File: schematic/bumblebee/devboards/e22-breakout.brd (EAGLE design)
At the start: 100 x 80 mm, 3 parts

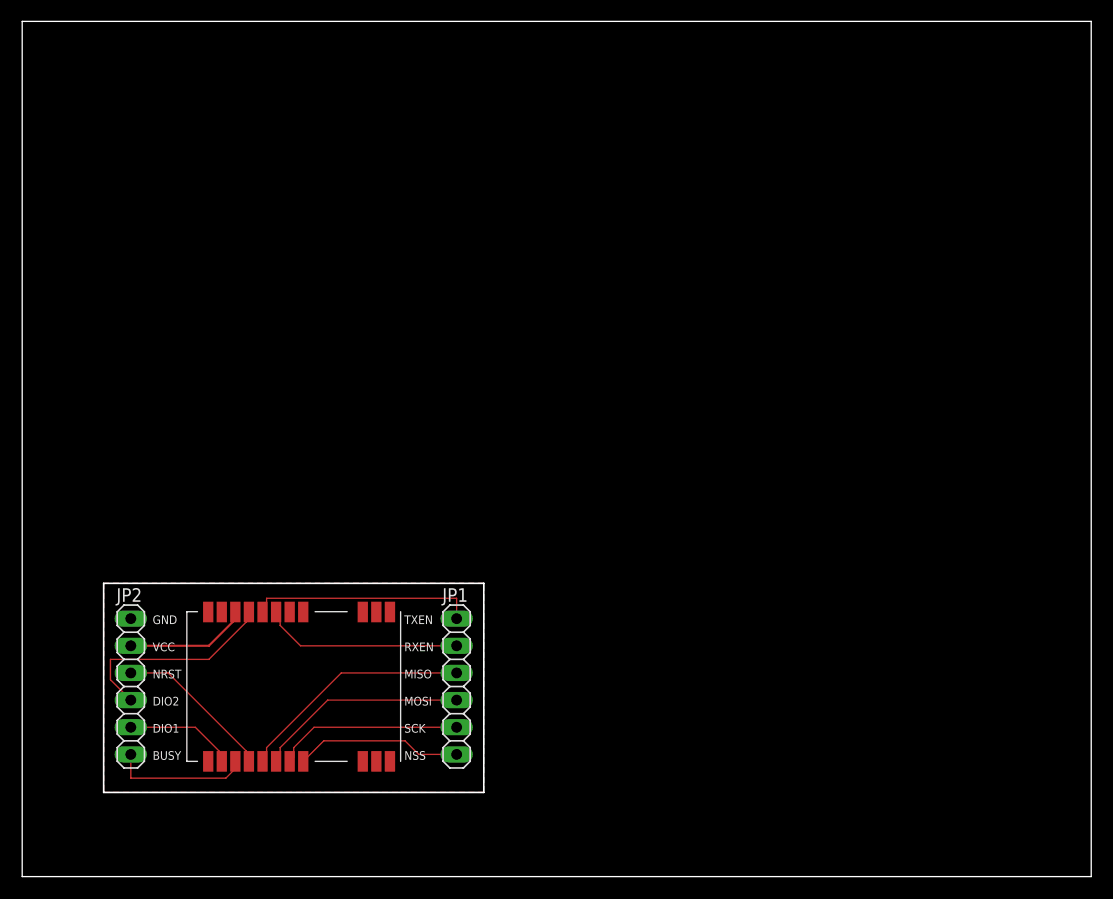
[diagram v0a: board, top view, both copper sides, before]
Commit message: Допилы брейкаута для радио и брейкаут для иридиума
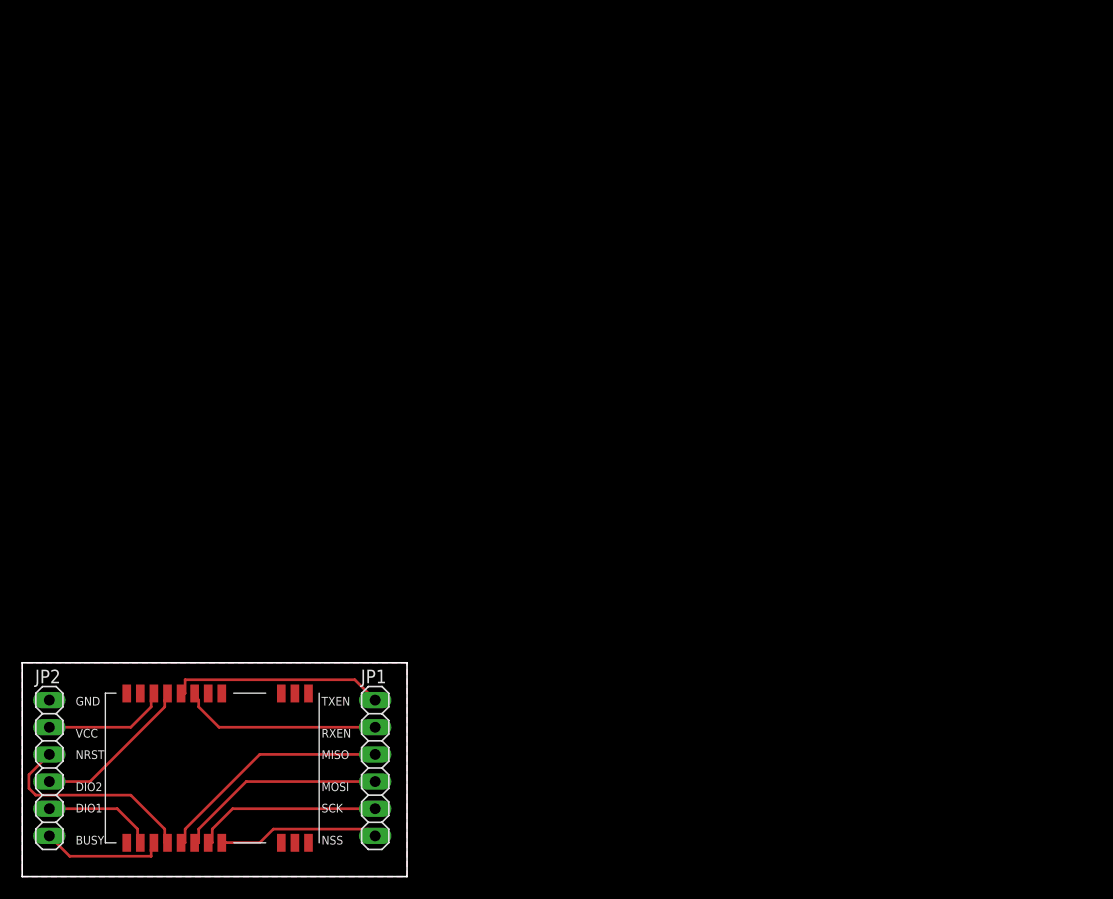
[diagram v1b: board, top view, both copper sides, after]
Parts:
- moved JP2 10.8 mm to (2.54, 10.2)
- moved JP1 10.8 mm to (33.0, 10.2)
- moved U$1 10.8 mm to (17.8, 10.2)
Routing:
- net DIO2: track 19.8 -> 15.0 mm
- net NRST: track 15.0 -> 19.8 mm
- net NSS: track 16.9 -> 15.1 mm
- net BUSY: track 13.0 -> 11.6 mm
- net TXEN: track 21.2 -> 20.2 mm
- added copper zone on layer 16, net GND
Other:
- board size 100 x 80 mm -> 36 x 20 mm

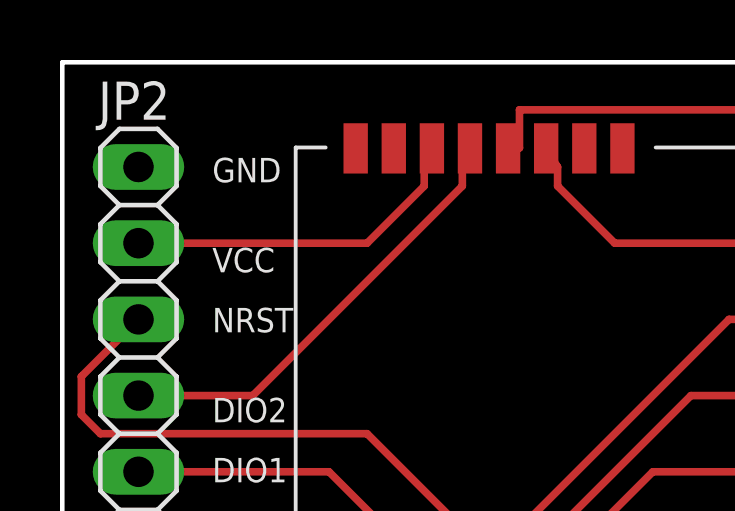
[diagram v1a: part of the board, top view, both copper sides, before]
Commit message: собираем все платы в один шаблон
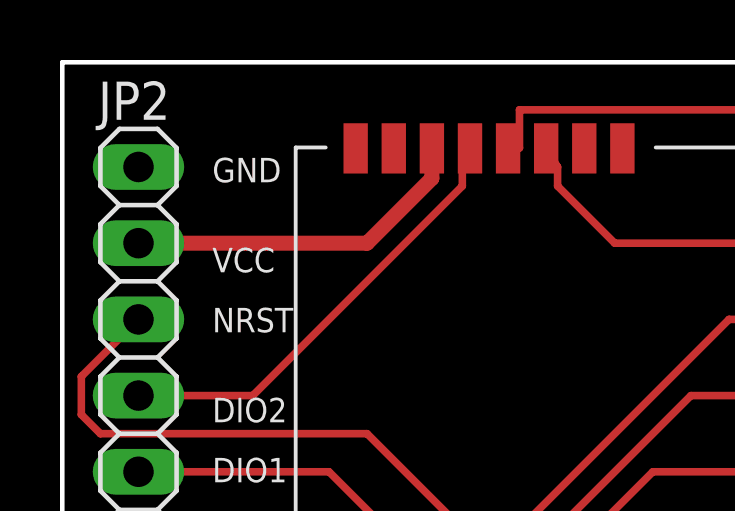
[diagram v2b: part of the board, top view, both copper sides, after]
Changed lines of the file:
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@@
 </variantdefs>
 <classes>
-<class number="0" name="default" width="0.125" drill="0">
+<class number="0" name="default" width="0.2" drill="0.5">
+<clearance class="0" value="0.2"/>
 </class>
-<class number="1" name="power" width="0.2" drill="0">
+<class number="1" name="power" width="0.2" drill="0.5">
+<clearance class="1" value="0.2"/>
 </class>
 </classes>
@@
 <contactref element="U$1" pad="P$9"/>
 <contactref element="JP2" pad="2"/>
-<wire x1="12.065" y1="15.875" x2="12.065" y2="16.51" width="0.254" layer="1"/>
-<wire x1="10.16" y1="13.97" x2="12.065" y2="15.875" width="0.254" layer="1"/>
-<wire x1="2.54" y1="13.97" x2="10.16" y2="13.97" width="0.254" layer="1"/>
-<wire x1="12.065" y1="16.51" x2="12.32" y2="17.13" width="0.254" layer="1"/>
+<wire x1="10.16" y1="13.97" x2="12.32" y2="16.13" width="0.5" layer="1"/>
+<wire x1="2.54" y1="13.97" x2="10.16" y2="13.97" width="0.5" layer="1"/>
+<wire x1="12.32" y1="16.13" x2="12.32" y2="17.13" width="0.5" layer="1"/>
 </signal>
 <signal name="NRST">
